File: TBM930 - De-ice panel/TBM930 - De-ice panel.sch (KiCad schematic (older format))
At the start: 67 parts, among them J1 USB_B_Micro, J10 AVR-ISP-6, J2 Barrel_Jack, J3 SW_AIRFRAME_DE_ICE, J4 SW_ICE_LIGHT, J5 SW_PROP_DE_ICE, J6 SW_WIND_SHIELD, J7 SW_PITOT_L_HTR, J8 SW_PITOT_R_HTR, J9 SW_INERT_SEP, SW1 SW_Push, SW2 SW_Push, U1 ATmega16U4-MU-Exposed-Extra-P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, U2 TLC5917IN, U3 TLC5917IN, Y1 16MHz

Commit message: More atmega32u4 routing
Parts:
- removed C8: 1uF, Capacitor_SMD:C_0603_1608Metric, symbol Device:C
- removed NT1: Net-Tie_2, NetTie:NetTie-2_SMD_Pad0.5mm, symbol Device:Net-Tie_2
- removed U1: ATmega16U4-MU-Exposed-Extra-Pins, Package_DFN_QFN:QFN-44-1EP_7x7mm_P0.5mm_EP5.2x5.2mm, symbol Global_MobiFlight_panel_parts:ATmega16U4-MU-Exposed-Extra-Pins
- added C1: 10uF, Capacitor_SMD:C_0603_1608Metric, symbol Device:C
- added C2, C3, C4: 0.1uF, Capacitor_SMD:C_0603_1608Metric, symbol Device:C
- added U3: ATmega32U4-MU, Package_DFN_QFN:QFN-44-1EP_7x7mm_P0.5mm_EP5.2x5.2mm, symbol Global_MobiFlight_panel_parts:ATmega32U4-MU
- C16: renamed from C3; footprint Capacitor_SMD:C_0603_1608Metric -> Capacitor_SMD:C_0402_1005Metric; JLC 0603 -> 0402; LCSC C1648 -> C1555
- C17: renamed from C4; footprint Capacitor_SMD:C_0603_1608Metric -> Capacitor_SMD:C_0402_1005Metric; JLC 0603 -> 0402; LCSC C1648 -> C1555
- D1: renamed from D2; value LED -> YELLOW; LCSC C2290 -> C72038
- D10: renamed from D16; footprint LED_SMD:LED_0603_1608Metric -> LED_SMD:LED_1206_3216Metric_Pad1.42x1.75mm_HandSolder; JLC LED_0603 -> (none); LCSC C2290 -> (none)
- D11: renamed from D23; footprint LED_SMD:LED_0603_1608Metric -> LED_SMD:LED_1206_3216Metric_Pad1.42x1.75mm_HandSolder; JLC LED_0603 -> (none); LCSC C2290 -> (none)
- D12: renamed from D10; footprint LED_SMD:LED_0603_1608Metric -> LED_SMD:LED_1206_3216Metric_Pad1.42x1.75mm_HandSolder; JLC LED_0603 -> (none); LCSC C2290 -> (none)
- D13: renamed from D17; footprint LED_SMD:LED_0603_1608Metric -> LED_SMD:LED_1206_3216Metric_Pad1.42x1.75mm_HandSolder; JLC LED_0603 -> (none); LCSC C2290 -> (none)
- D14: renamed from D24; footprint LED_SMD:LED_0603_1608Metric -> LED_SMD:LED_1206_3216Metric_Pad1.42x1.75mm_HandSolder; JLC LED_0603 -> (none); LCSC C2290 -> (none)
- D15: renamed from D11; footprint LED_SMD:LED_0603_1608Metric -> LED_SMD:LED_1206_3216Metric_Pad1.42x1.75mm_HandSolder; JLC LED_0603 -> (none); LCSC C2290 -> (none)
- D16: renamed from D18; footprint LED_SMD:LED_0603_1608Metric -> LED_SMD:LED_1206_3216Metric_Pad1.42x1.75mm_HandSolder; JLC LED_0603 -> (none); LCSC C2290 -> (none)
- D17: renamed from D25; footprint LED_SMD:LED_0603_1608Metric -> LED_SMD:LED_1206_3216Metric_Pad1.42x1.75mm_HandSolder; JLC LED_0603 -> (none); LCSC C2290 -> (none)
- D18: renamed from D12; footprint LED_SMD:LED_0603_1608Metric -> LED_SMD:LED_1206_3216Metric_Pad1.42x1.75mm_HandSolder; JLC LED_0603 -> (none); LCSC C2290 -> (none)
- D19, D9: footprint LED_SMD:LED_0603_1608Metric -> LED_SMD:LED_1206_3216Metric_Pad1.42x1.75mm_HandSolder; JLC LED_0603 -> (none); LCSC C2290 -> (none)
- D2: renamed from D3; value LED -> GREEN; LCSC C2290 -> C2297
- D20: renamed from D26; footprint LED_SMD:LED_0603_1608Metric -> LED_SMD:LED_1206_3216Metric_Pad1.42x1.75mm_HandSolder; JLC LED_0603 -> (none); LCSC C2290 -> (none)
- D21: renamed from D13; footprint LED_SMD:LED_0603_1608Metric -> LED_SMD:LED_1206_3216Metric_Pad1.42x1.75mm_HandSolder; JLC LED_0603 -> (none); LCSC C2290 -> (none)
- D22: renamed from D20; footprint LED_SMD:LED_0603_1608Metric -> LED_SMD:LED_1206_3216Metric_Pad1.42x1.75mm_HandSolder; JLC LED_0603 -> (none); LCSC C2290 -> (none)
- D23: renamed from D27; footprint LED_SMD:LED_0603_1608Metric -> LED_SMD:LED_1206_3216Metric_Pad1.42x1.75mm_HandSolder; JLC LED_0603 -> (none); LCSC C2290 -> (none)
- D24: renamed from D14; footprint LED_SMD:LED_0603_1608Metric -> LED_SMD:LED_1206_3216Metric_Pad1.42x1.75mm_HandSolder; JLC LED_0603 -> (none); LCSC C2290 -> (none)
- D25: renamed from D21; footprint LED_SMD:LED_0603_1608Metric -> LED_SMD:LED_1206_3216Metric_Pad1.42x1.75mm_HandSolder; JLC LED_0603 -> (none); LCSC C2290 -> (none)
- D26: renamed from D15; footprint LED_SMD:LED_0603_1608Metric -> LED_SMD:LED_1206_3216Metric_Pad1.42x1.75mm_HandSolder; JLC LED_0603 -> (none); LCSC C2290 -> (none)
- D27: renamed from D22; footprint LED_SMD:LED_0603_1608Metric -> LED_SMD:LED_1206_3216Metric_Pad1.42x1.75mm_HandSolder; JLC LED_0603 -> (none); LCSC C2290 -> (none)
- D3: renamed from D1; value LED -> GREEN; LCSC C2290 -> C2297
- J10: footprint Connector_PinHeader_1.00mm:PinHeader_1x06_P1.00mm_Vertical -> Connector_PinHeader_2.54mm:PinHeader_2x03_P2.54mm_Vertical
- R2: renamed from R5; footprint Resistor_SMD:R_0603_1608Metric -> Resistor_SMD:R_0201_0603Metric
- R5: renamed from R6; footprint Resistor_SMD:R_0603_1608Metric -> Resistor_SMD:R_0201_0603Metric
- renumbered C5 to C10, C6 to C11, C7 to C12, C10 to C13, C11 to C14, C12 to C15, C9 to C5, C1 to C6, C2 to C7, C13 to C8, C14 to C9, J3 to J1, J4 to J2, J5 to J3, J6 to J4, J7 to J5, J8 to J6, J9 to J7, J2 to J8, J1 to J9, R7 to R3, R8 to R4, R4 to R6, R2 to R7, R3 to R8, SW2 to SW1, SW1 to SW2, U2 to U1, U3 to U2
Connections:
- net labels added: DR+, DR-
- wire segments 114 -> 121
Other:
- note added: "Labels"
- note added: "Perimiter backlight"
- moved on the sheet: C5, C8, C9, D10, D11, D12, D13, D14, D15, D16, D17, D18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

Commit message: Everything is routed!
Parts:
- removed C11, C14: 1uF, Capacitor_SMD:C_0603_1608Metric, symbol Device:C
- removed C12, C15: 0.1uF, Capacitor_SMD:C_0603_1608Metric, symbol Device:C
- removed C13: 10uF, Capacitor_SMD:C_0603_1608Metric, symbol Device:CP
- removed D17: LED, LED_SMD:LED_1206_3216Metric_Pad1.42x1.75mm_HandSolder, symbol Device:LED
- removed FB1: Ferrite_Bead, Resistor_SMD:R_0805_2012Metric, symbol Device:Ferrite_Bead
- removed Y1: 16MHz, Crystal:Crystal_SMD_3225-4Pin_3.2x2.5mm, symbol Device:Crystal
- added FB1: Ferrite_Bead_Small, Capacitor_SMD:C_0805_2012Metric, symbol Device:Ferrite_Bead_Small
- added R9: 330, Resistor_SMD:R_0603_1608Metric, symbol Device:R
- added Y1: Crystal_GND24, Crystal:Crystal_SMD_3225-4Pin_3.2x2.5mm, symbol Global_MobiFlight_panel_parts:Crystal_GND24
- R2, R5: footprint Resistor_SMD:R_0201_0603Metric -> Resistor_SMD:R_0603_1608Metric
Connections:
- net labels removed: +12V
- wire segments 121 -> 115
- no-connect marks 13 -> 12
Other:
- moved on the sheet: SW2

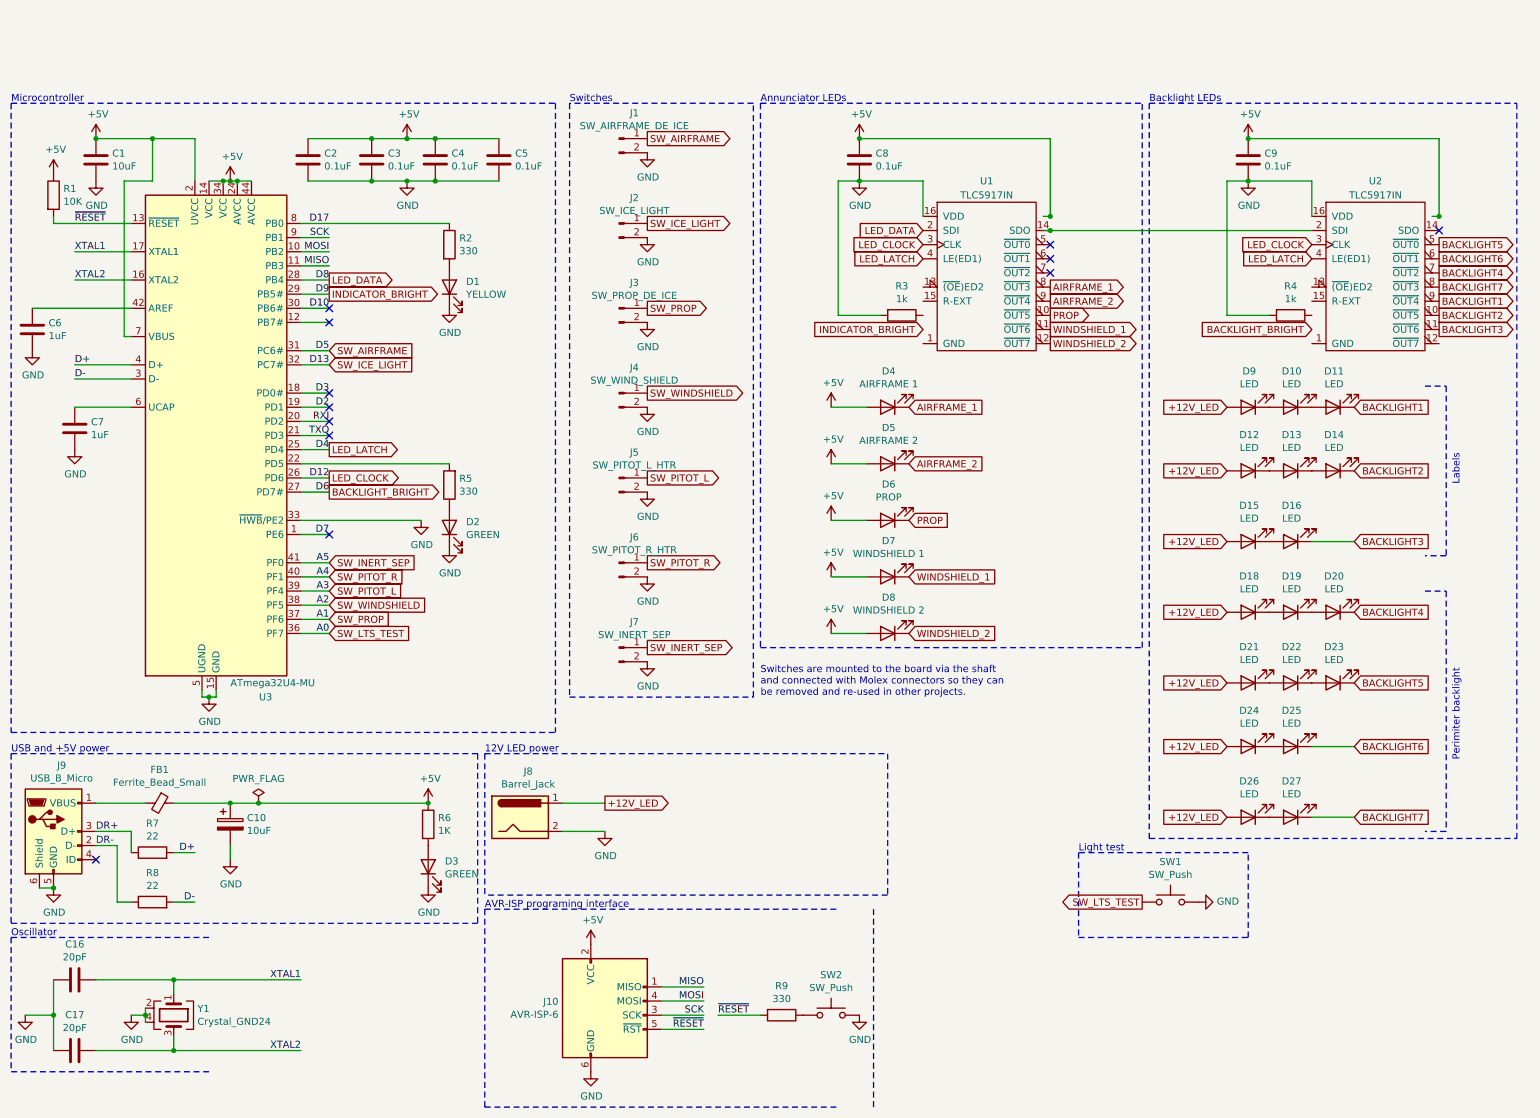
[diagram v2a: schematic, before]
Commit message: Schematic submitted to microtype
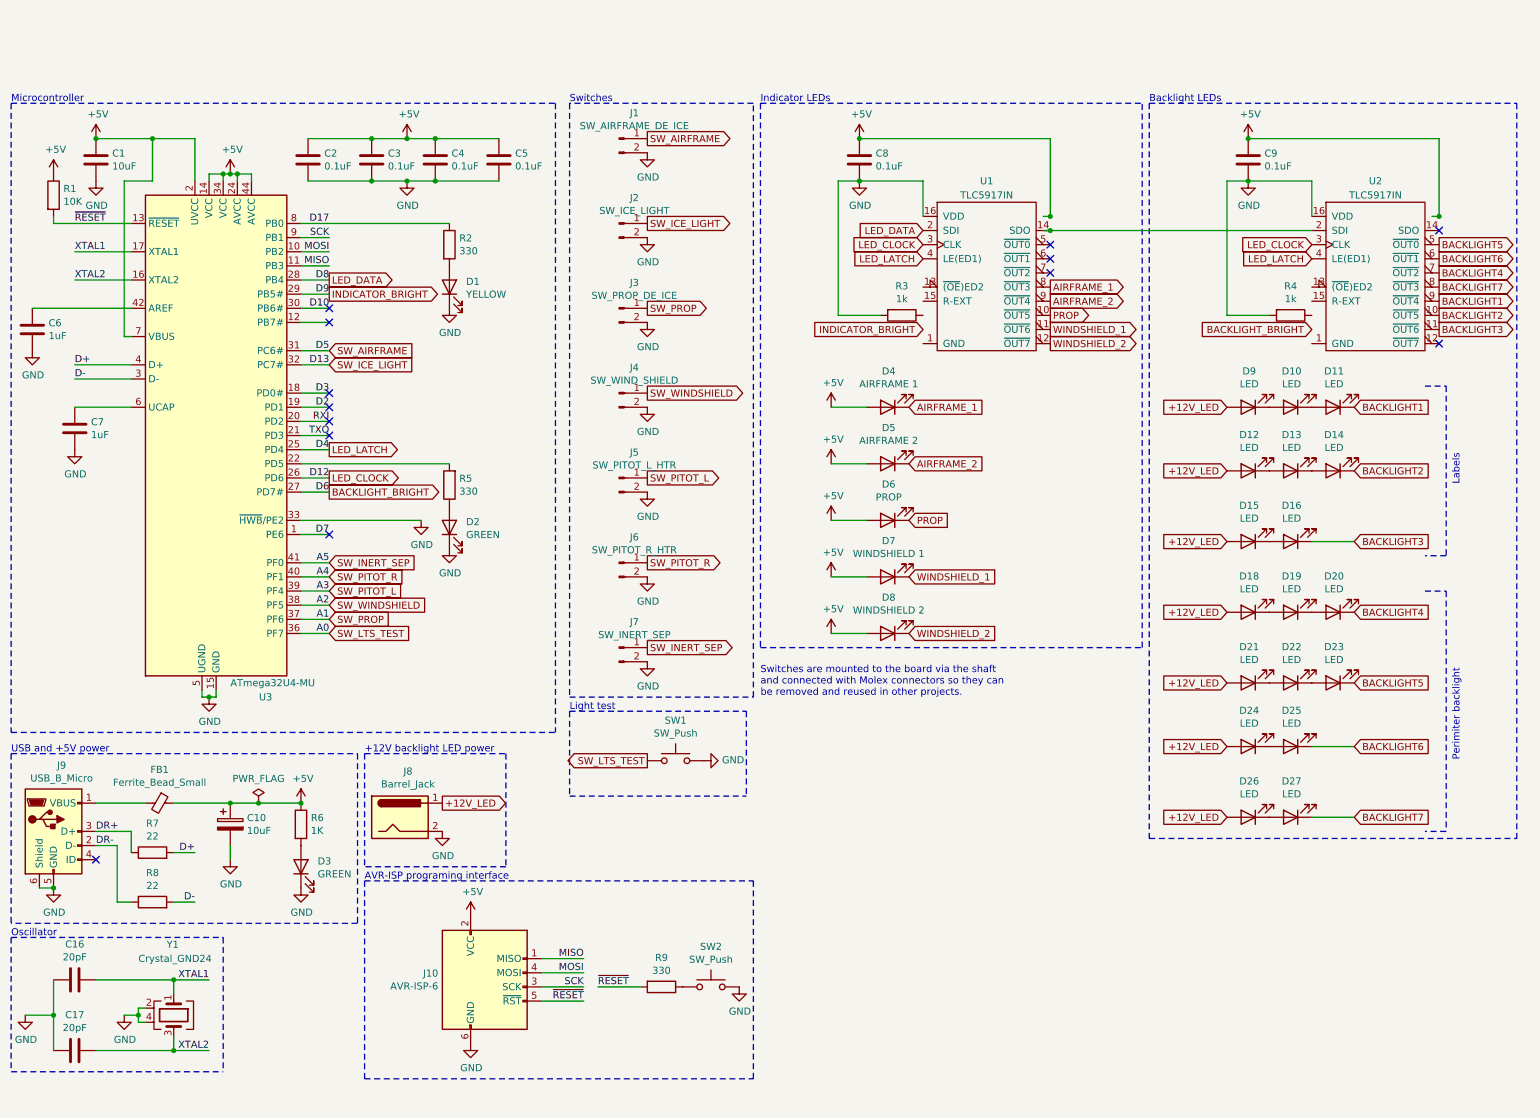
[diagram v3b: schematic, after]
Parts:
- D2, D3: LCSC C2297 -> C72043
- D4: JLC SMD-CRY-3225_4P -> (none); LCSC C13738 -> (none)
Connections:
- no-connect marks 12 -> 13
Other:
- note added: "+12V backlight LED power"
- note added: "Indicator LEDs"
- note added: "Switches are mounted to the board via the shaft\nand connected with Molex connectors so they can\nbe removed and reused in other projects.\n"
- note removed: "12V LED power"
- note removed: "Annunciator LEDs"
- note removed: "Switches are mounted to the board via the shaft\nand connected with Molex connectors so they can\nbe removed and re-used in other projects.\n"
- moved on the sheet: D3, J10, J8, R6, R9, SW1, SW2

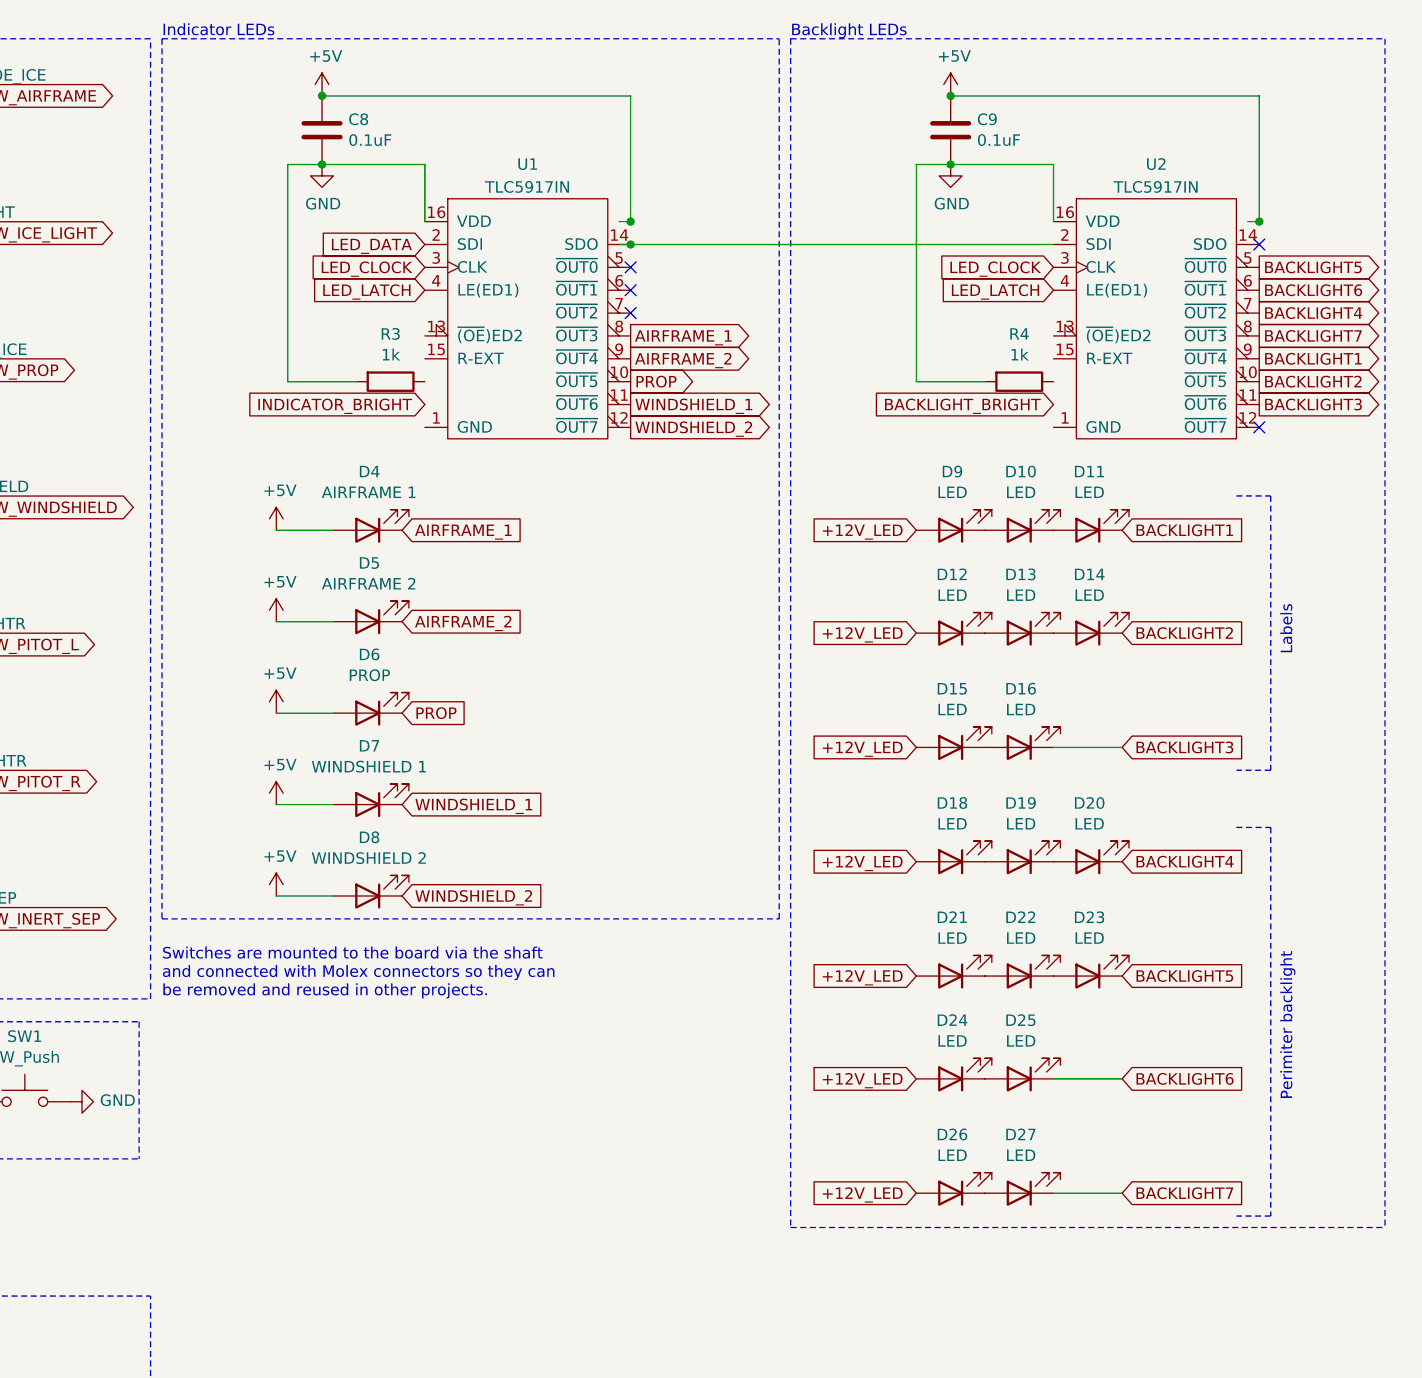
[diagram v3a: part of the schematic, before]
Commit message: Schematic updates based on MT engineering discord feedback
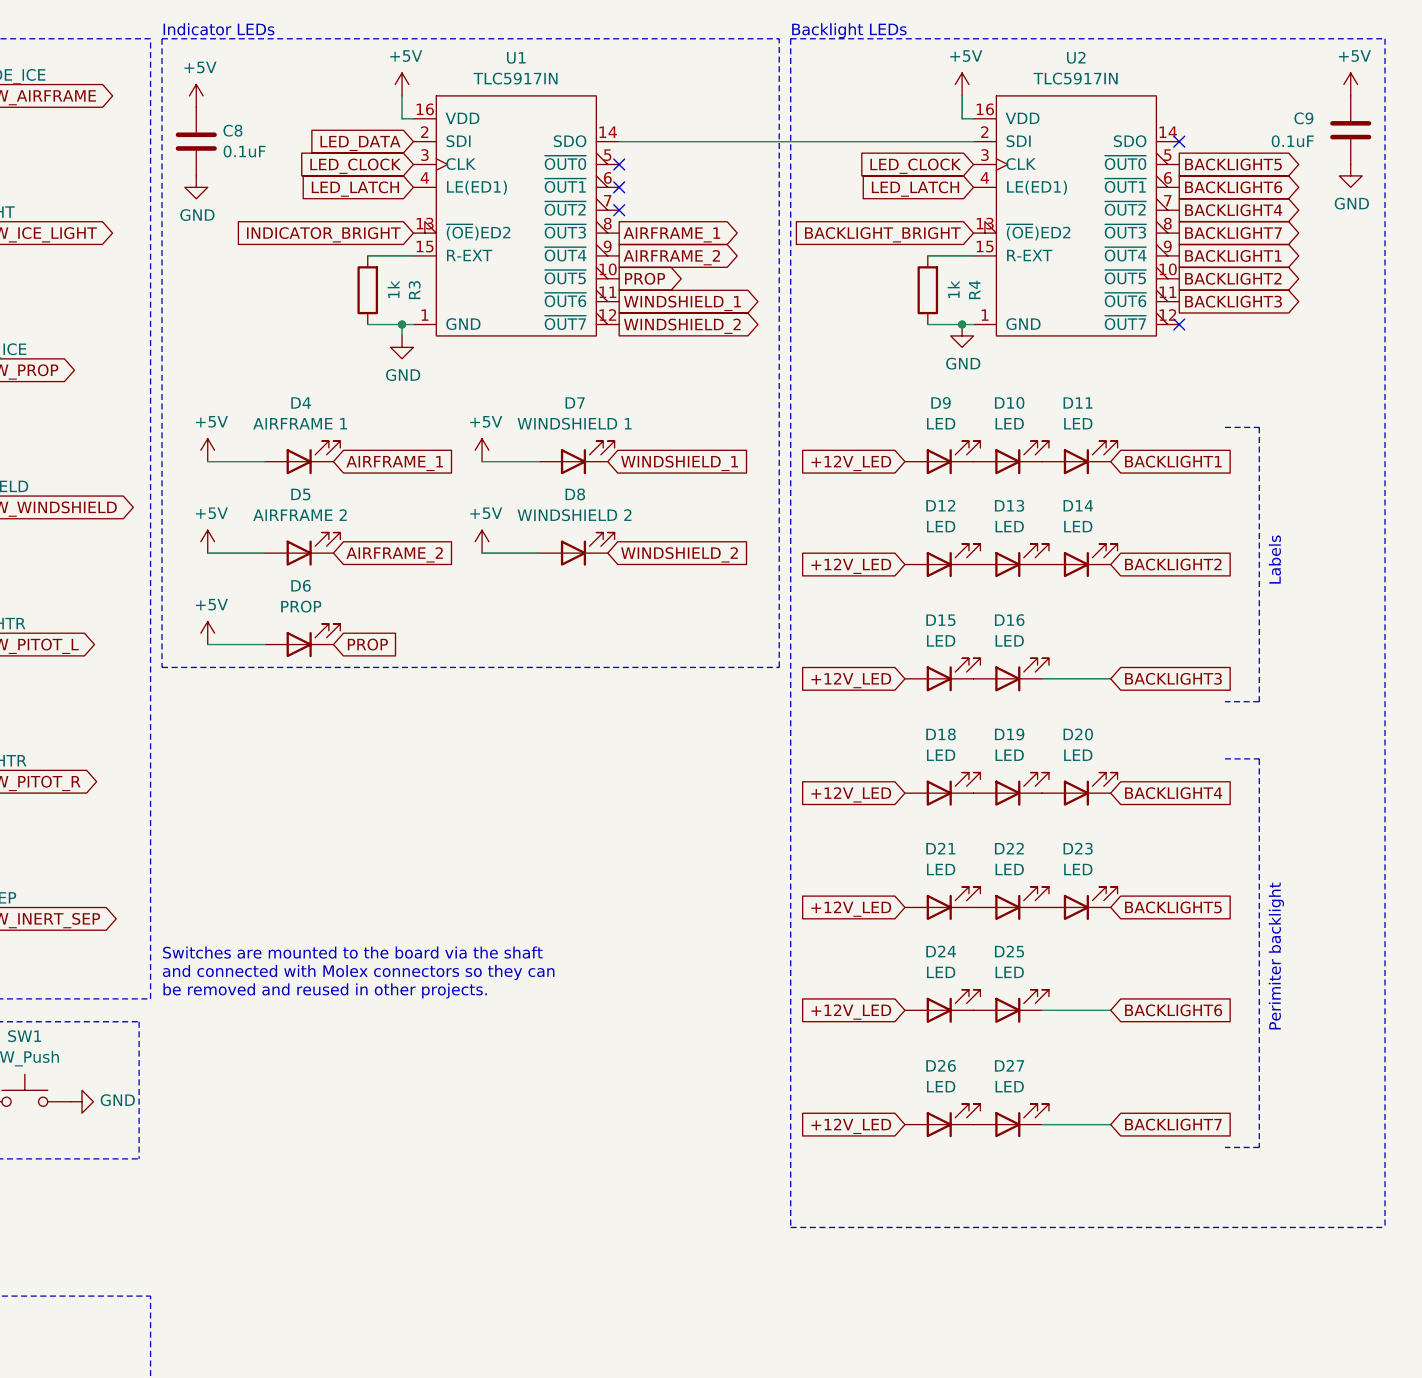
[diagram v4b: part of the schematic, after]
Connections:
- net +5V: now also U1.16 (VDD), U2.16 (VDD)
- net BACKLIGHT_BRIGHT: now also U2.13 (~(OE)ED2)
- net GND: now also R3.1, R4.1, U1.1 (GND), U2.1 (GND); no longer R3.2, R4.2, U1.16 (VDD), U2.16 (VDD)
- net INDICATOR_BRIGHT: now also U1.13 (~(OE)ED2)
- net at U2.15 (R-EXT): now also R4.2
- net at U1.15 (R-EXT): now also R3.2
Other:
- moved on the sheet: C8, C9, D10, D11, D12, D13, D14, D15, D16, D18, D19, D20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
